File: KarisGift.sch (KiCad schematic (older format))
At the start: 39 parts

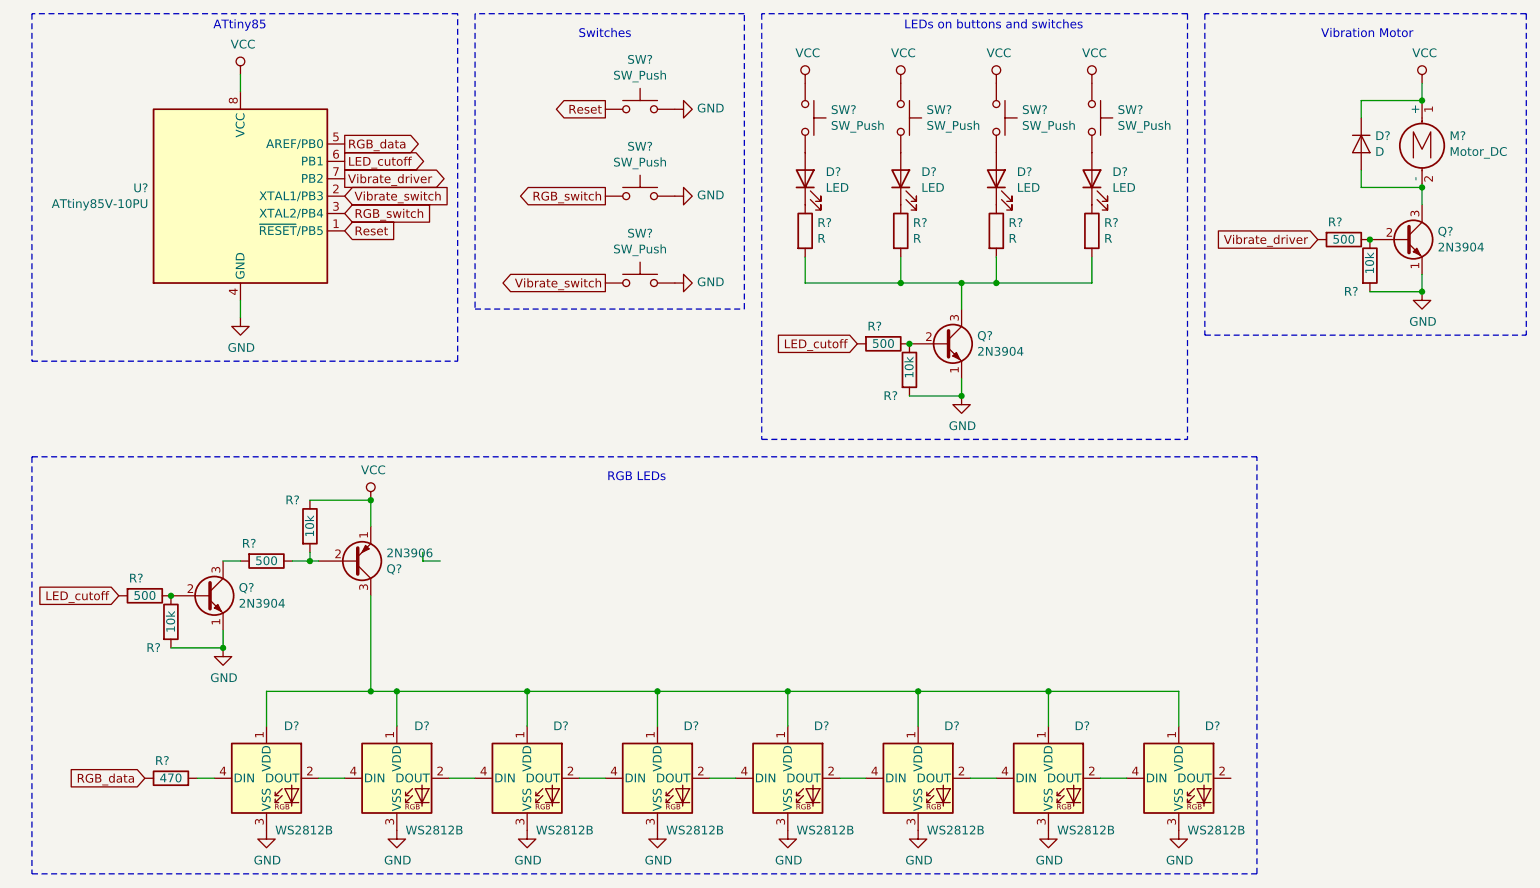
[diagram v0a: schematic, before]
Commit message: Added footprints to all parts in schematic.
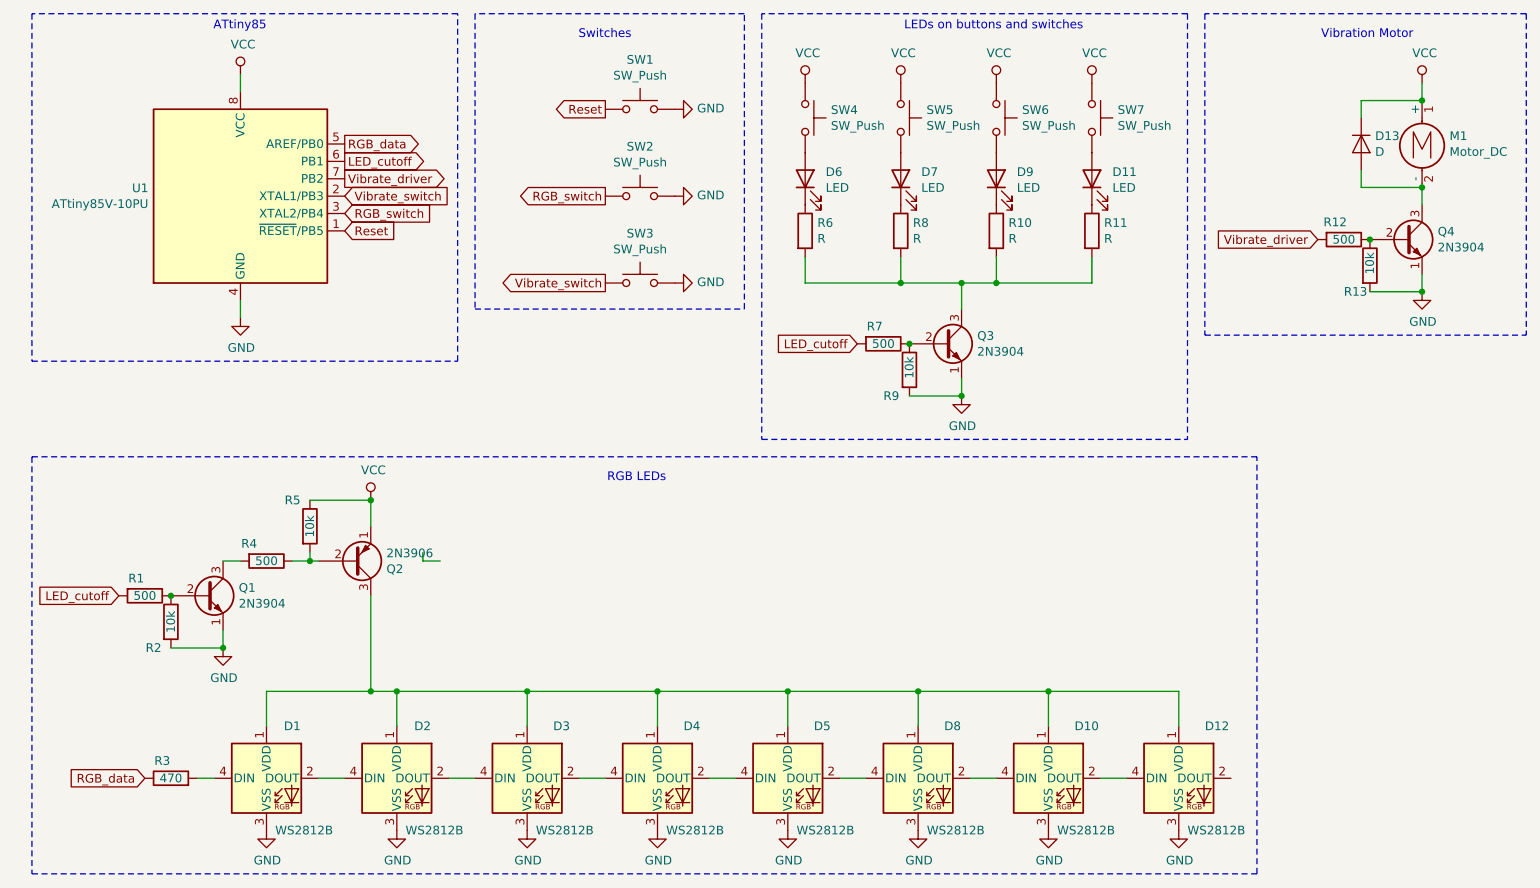
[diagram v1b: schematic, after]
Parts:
- gave numbers to parts that had none: 39
